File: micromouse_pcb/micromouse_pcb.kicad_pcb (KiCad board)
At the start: 2 copper layers, 7 parts, among them J101 Conn_01x03, J102 Conn_01x06, J103 Conn_02x20_Odd_Even, J104 Conn_01x02, J105 Conn_01x02, J106 Conn_01x02, U101 Teensy4.1

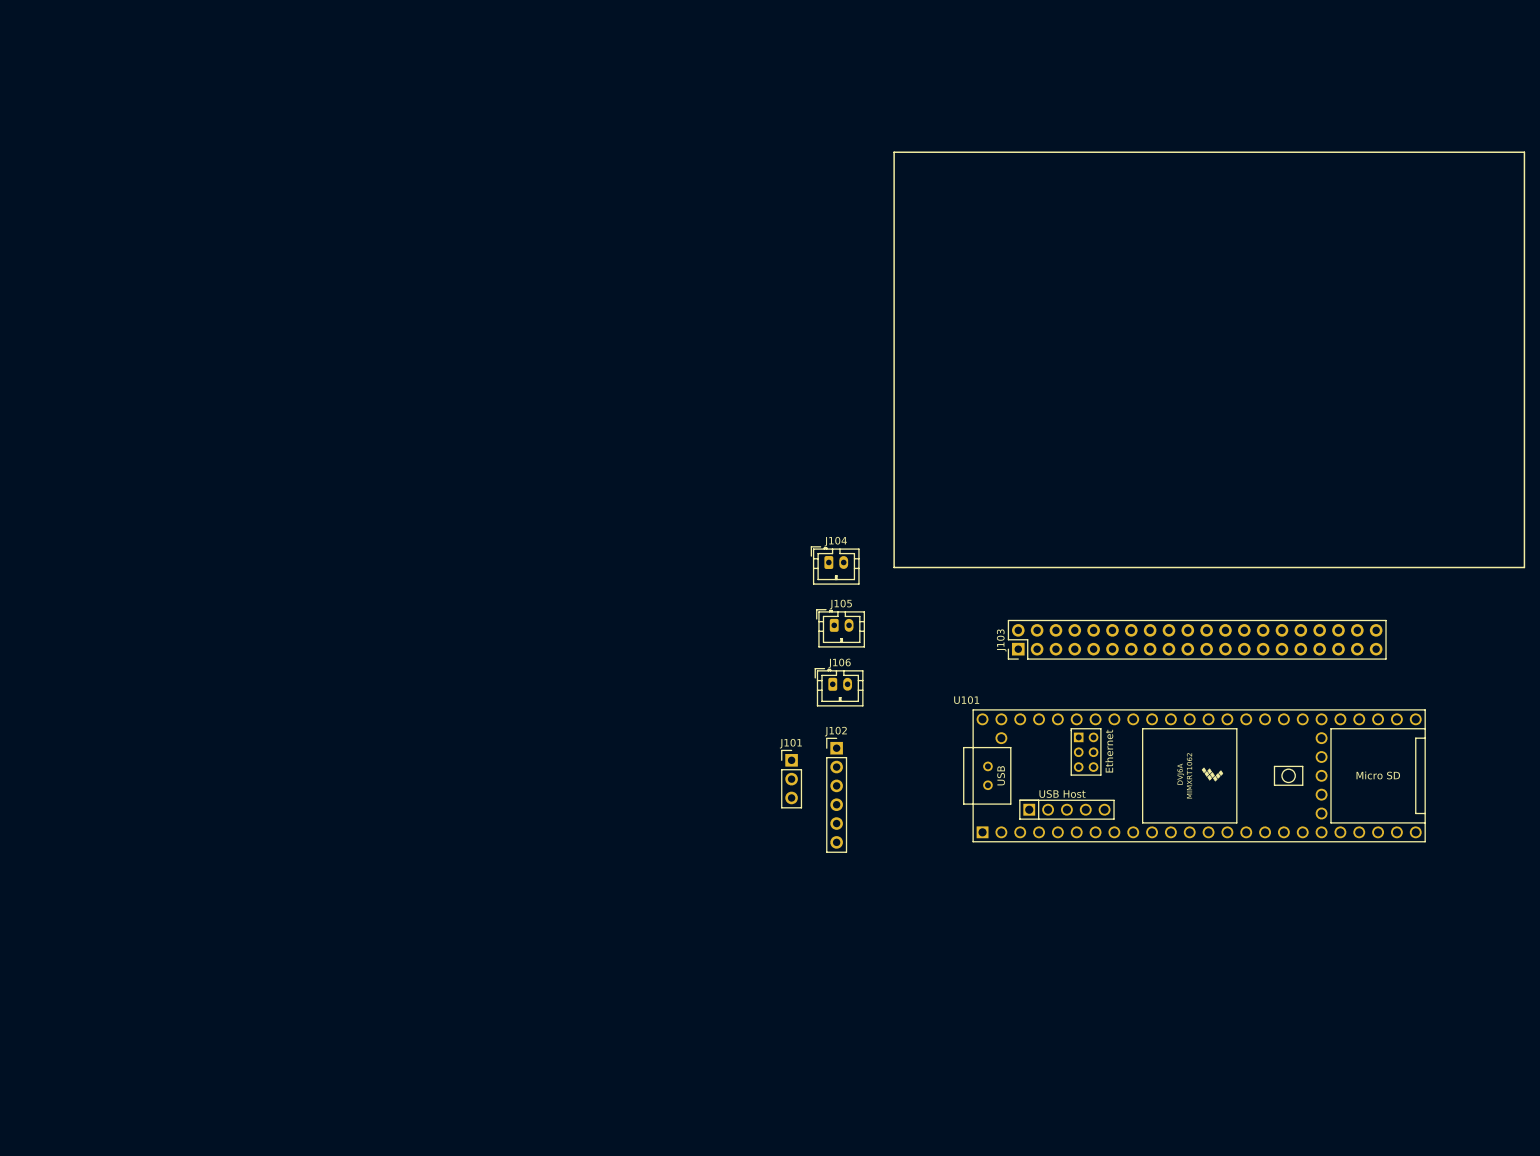
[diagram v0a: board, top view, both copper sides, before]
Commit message: added regulators and motor encoders schematic
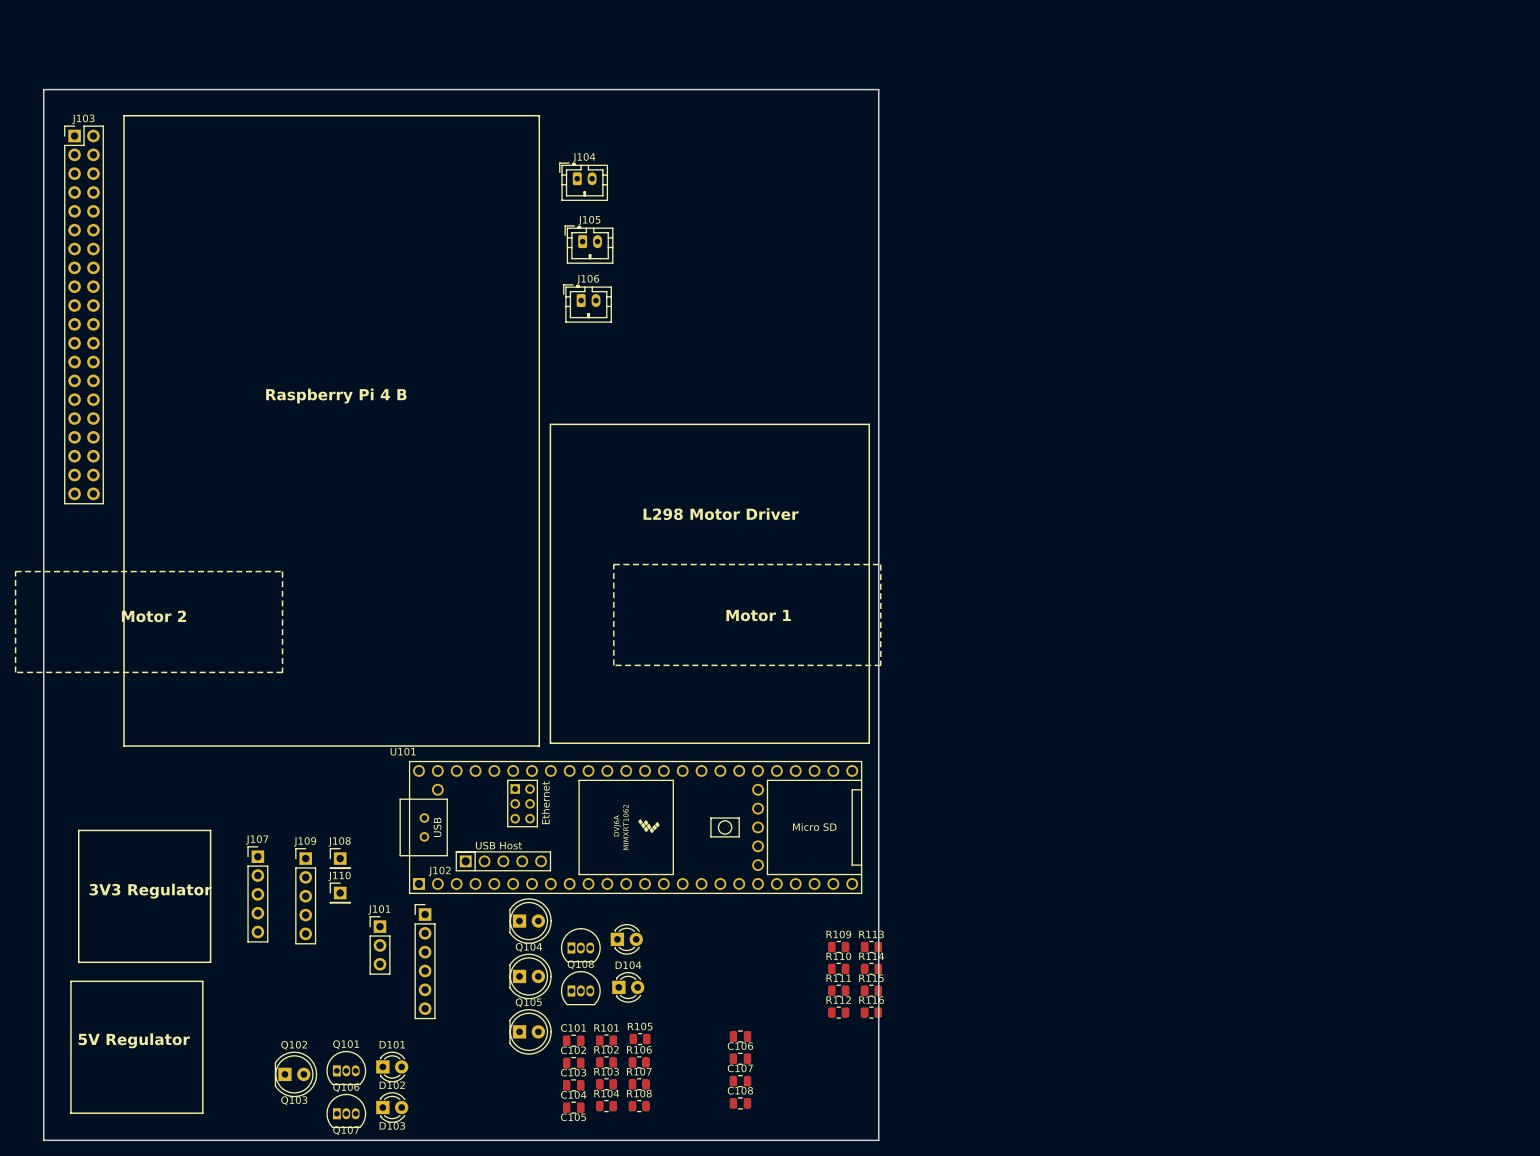
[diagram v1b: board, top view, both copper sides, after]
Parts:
- added C101: 4.7 uF, Capacitor_SMD:C_0805_2012Metric, F.Cu at (124.1, 150.9)
- added C102: 0.1 uF, Capacitor_SMD:C_0805_2012Metric, F.Cu at (124.1, 153.9)
- added C103: 4.7 uF, Capacitor_SMD:C_0805_2012Metric, F.Cu at (124.1, 157.0)
- added C104: 0.1 uF, Capacitor_SMD:C_0805_2012Metric, F.Cu at (124.1, 160.0)
- added C105: 4.7 uF, Capacitor_SMD:C_0805_2012Metric, F.Cu at (146.6, 150.4)
- added C106: 0.1 uF, Capacitor_SMD:C_0805_2012Metric, F.Cu at (146.6, 153.4)
- added C107: 4.7 uF, Capacitor_SMD:C_0805_2012Metric, F.Cu at (146.6, 156.4)
- added C108: 0.1 uF, Capacitor_SMD:C_0805_2012Metric, F.Cu at (146.6, 159.4)
- added D101: INL-5AMIR15, LED_THT:LED_D3.0mm_IRBlack, F.Cu at (98.4, 154.5)
- added D102: INL-5AMIR15, LED_THT:LED_D3.0mm_IRBlack, F.Cu at (98.4, 159.9)
- added D103: INL-5AMIR15, LED_THT:LED_D3.0mm_IRBlack, F.Cu at (130.0, 137.3)
- added D104: INL-5AMIR15, LED_THT:LED_D3.0mm_IRBlack, F.Cu at (130.2, 143.8)
- added J107: Conn_01x05, Connector_PinHeader_2.54mm:PinHeader_1x05_P2.54mm_Vertical, F.Cu at (81.5, 126.1)
- added J108: Conn_01x01, Connector_PinHeader_2.54mm:PinHeader_1x01_P2.54mm_Vertical, F.Cu at (92.7, 126.4)
- added J109: Conn_01x05, Connector_PinHeader_2.54mm:PinHeader_1x05_P2.54mm_Vertical, F.Cu at (88.0, 126.4)
- added J110: Conn_01x01, Connector_PinHeader_2.54mm:PinHeader_1x01_P2.54mm_Vertical, F.Cu at (92.7, 131.0)
- added Q101: BS170, Package_TO_SOT_THT:TO-92_Inline, F.Cu at (92.2, 155.0)
- added Q102: SFH313FA, LED_THT:LED_D5.0mm_Clear, F.Cu at (85.2, 155.5)
- added Q103: SFH313FA, LED_THT:LED_D5.0mm_Clear, F.Cu at (116.8, 134.8)
- added Q104: SFH313FA, LED_THT:LED_D5.0mm_Clear, F.Cu at (116.8, 142.3)
- added Q105: SFH313FA, LED_THT:LED_D5.0mm_Clear, F.Cu at (116.8, 149.7)
- added Q106: BS170, Package_TO_SOT_THT:TO-92_Inline, F.Cu at (92.2, 160.8)
- added Q107: BS170, Package_TO_SOT_THT:TO-92_Inline, F.Cu at (123.8, 138.4)
- added Q108: BS170, Package_TO_SOT_THT:TO-92_Inline, F.Cu at (123.8, 144.2)
- added R101: 100, Resistor_SMD:R_0805_2012Metric, F.Cu at (128.6, 150.9)
- added R102: 47K, Resistor_SMD:R_0805_2012Metric, F.Cu at (128.6, 153.9)
- added R103: 50 Ohm, Resistor_SMD:R_0805_2012Metric, F.Cu at (128.6, 156.8)
- added R104: 1.8k, Resistor_SMD:R_0805_2012Metric, F.Cu at (128.6, 159.8)
- added R105: 1.8k, Resistor_SMD:R_0805_2012Metric, F.Cu at (133.1, 150.7)
- added R106: 1.8k, Resistor_SMD:R_0805_2012Metric, F.Cu at (133.0, 153.9)
- added R107: 1.8k, Resistor_SMD:R_0805_2012Metric, F.Cu at (133.0, 156.8)
- added R108: 100, Resistor_SMD:R_0805_2012Metric, F.Cu at (133.0, 159.8)
- added R109: 47K, Resistor_SMD:R_0805_2012Metric, F.Cu at (159.9, 138.3)
- added R110: 50 Ohm, Resistor_SMD:R_0805_2012Metric, F.Cu at (159.9, 141.2)
- added R111: 100, Resistor_SMD:R_0805_2012Metric, F.Cu at (159.9, 144.2)
- added R112: 47K, Resistor_SMD:R_0805_2012Metric, F.Cu at (159.9, 147.2)
- added R113: 50 Ohm, Resistor_SMD:R_0805_2012Metric, F.Cu at (164.3, 138.3)
- added R114: 100, Resistor_SMD:R_0805_2012Metric, F.Cu at (164.3, 141.2)
- added R115: 47K, Resistor_SMD:R_0805_2012Metric, F.Cu at (164.3, 144.2)
- added R116: 50 Ohm, Resistor_SMD:R_0805_2012Metric, F.Cu at (164.3, 147.2)
- moved J103 144.9 mm to (56.8, 28.9), turned to 0 degrees
- moved U101 76.3 mm to (128.4, 122.3)
- moved J104 61.9 mm to (124.6, 34.7)
- moved J105 61.9 mm to (125.3, 43.2)
- moved J106 61.9 mm to (125.2, 51.1)
- moved J101 59.9 mm to (98.0, 135.6)
- moved J102 59.9 mm to (104.1, 133.9)
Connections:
- J101 pad 3: /VIN -> /VBAT
- J106 pad 1: Net-(J105-Pin_2) -> Net-(J104-Pin_2)
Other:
- board outline added: 112.6 x 141.7 mm
- board text added: "3V3 Regulator"
- board text added: "5V Regulator"
- board text added: "L298 Motor Driver"
- board text added: "Motor 1"
- board text added: "Motor 2"
- board text added: "Raspberry Pi 4 B"

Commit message: general board layout established v1
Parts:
- removed J107, J109: Conn_01x05, Connector_PinHeader_2.54mm:PinHeader_1x05_P2.54mm_Vertical
- removed J108, J110: Conn_01x01, Connector_PinHeader_2.54mm:PinHeader_1x01_P2.54mm_Vertical
- added H101: MountingHole_Pad, MountingHole:MountingHole_2.2mm_M2_DIN965_Pad, F.Cu at (162.7, 58.5)
- added H102: MountingHole_Pad, MountingHole:MountingHole_2.2mm_M2_DIN965_Pad, F.Cu at (149.3, 53.2)
- added H103: MountingHole_Pad, MountingHole:MountingHole_2.2mm_M2_DIN965_Pad, F.Cu at (162.5, 40.1)
- added H104: MountingHole_Pad, MountingHole:MountingHole_2.2mm_M2_DIN965_Pad, F.Cu at (149.5, 71.7)
- added H105: MountingHole_Pad, MountingHole:MountingHole_2.2mm_M2_DIN965_Pad, F.Cu at (56.4, 75.3)
- added H106: MountingHole_Pad, MountingHole:MountingHole_2.2mm_M2_DIN965_Pad, F.Cu at (114.3, 26.4)
- added H107: MountingHole_Pad, MountingHole:MountingHole_2.2mm_M2_DIN965_Pad, F.Cu at (56.4, 26.4)
- added H108: MountingHole_Pad, MountingHole:MountingHole_2.2mm_M2_DIN965_Pad, F.Cu at (114.3, 75.3)
- added H109: MountingHole_Pad, MountingHole:MountingHole_3.2mm_M3_DIN965_Pad, F.Cu at (125.1, 119.5)
- added H110: MountingHole_Pad, MountingHole:MountingHole_3.2mm_M3_DIN965_Pad, F.Cu at (162.0, 119.5)
- added H111: MountingHole_Pad, MountingHole:MountingHole_3.2mm_M3_DIN965_Pad, F.Cu at (162.0, 82.6)
- added H112: MountingHole_Pad, MountingHole:MountingHole_3.2mm_M3_DIN965_Pad, F.Cu at (125.1, 82.6)
- added J111: Conn_01x06, Connector_PinHeader_2.54mm:PinHeader_1x06_P2.54mm_Vertical, F.Cu at (93.9, 88.9)
- added U102: ~, Regulator_Pololu_D24V22FX:D24V22FX, F.Cu at (166.5, 61.8)
- added U103: ~, Regulator_Pololu_D24V22FX:D24V22FX, F.Cu at (166.5, 43.2)
- J105: value Conn_01x02 -> Conn_01x06; footprint Connector_JST:JST_PH_B2B-PH-K_1x02_P2.00mm_Vertical -> Connector_PinHeader_2.54mm:PinHeader_1x06_P2.54mm_Vertical
- moved J103 81.5 mm to (60.3, 110.4), turned to 90 degrees
- moved R109 73.5 mm to (87.3, 149.8), turned to 90 degrees
- moved R110 72.4 mm to (89.5, 158.4), turned to -90 degrees
- moved R103 70.3 mm to (59.6, 143.6), turned to 180 degrees
- moved R104 65.1 mm to (64.1, 150.9), turned to 90 degrees
- moved C102 62.1 mm to (62.8, 144.3), turned to -90 degrees
- moved R101 61.5 mm to (68.5, 137.8)
- moved R102 61.3 mm to (68.5, 141.5)
- moved C101 58.9 mm to (65.6, 144.3), turned to -90 degrees
- moved R108 50.2 mm to (83.8, 149.9), turned to 90 degrees
- moved J105 49.0 mm to (107.8, 88.9)
- moved U101 46.7 mm to (81.8, 124.1)
- moved J102 46.5 mm to (149.9, 125.8), turned to 90 degrees
- moved Q105 44.6 mm to (159.8, 138.1), turned to 90 degrees
- moved J101 43.4 mm to (140.3, 125.9), turned to 90 degrees
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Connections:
- net Net-(J105-Pin_2) renamed /MOTOR1_OUTB
- J101 pad 1: /5V -> unconnected-(J101-Pin_1-Pad1)
- J105 pad 1: Net-(J104-Pin_2) -> GND
- U101 pad 48: unconnected-(U101-VIN-Pad48) -> /5V_REGULATED
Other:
- board text added: "L298N Motor Driver"
- board text added: "Raspberry Pi 4B"
- board text removed: "3V3 Regulator"
- board text removed: "5V Regulator"
- board text removed: "L298 Motor Driver"
- board text removed: "Raspberry Pi 4 B"
